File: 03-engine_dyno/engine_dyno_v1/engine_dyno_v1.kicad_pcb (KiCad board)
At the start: 4 copper layers, 101.3 x 69 mm, 91 parts, among them J1 Screw_Terminal_01x02, J4 Screw_Terminal_01x05, J5 Screw_Terminal_01x03, J6 Screw_Terminal_01x05, J7 Screw_Terminal_01x03, P1 J1B1211CCD, Q1 PMOS, U1 LMR51430XDDCR, U10 INA827AIDGKR, U11 74LVC1G17, U12 AD630ARZ, U13 ADS1120IPWR, U14 OPA192IDBVR, U15 OPA192IDBVR, U16 74LVC1G17, U2 TVS1800DRV, U3 TPS2115APWR, U4 TPS60403DBVRG4, U5 AD5689RBRUZ, U6 Teensy4.1, U7 INA827AIDGKR, U8 AD630ARZ, U9 ADS1120IPWR

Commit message: drc errors fixed
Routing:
- net /MCU/MOSI: track 78.0 -> 89.0 mm
- net Net-(U10-VOUT): track 32.2 -> 33.6 mm

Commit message: some silkscreen fancifications
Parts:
- moved C5 0.05 mm to (169.1, 86.9)
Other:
- outline, holes or cut-outs redrawn
- board text added: "EXC+"
- board text added: "EXC-"
- board text added: "MODEL1605 Input"
- board text added: "SIG+"
- board text added: "SIG-"

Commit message: im aboutta release
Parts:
- added H1: MountingHole, MountingHole:MountingHole_3.2mm_M3_DIN965, F.Cu at (108.5, 73.0)
- added H2: MountingHole, MountingHole:MountingHole_3.2mm_M3_DIN965, F.Cu at (108.7, 108.0)
- added H3: MountingHole, MountingHole:MountingHole_3.2mm_M3_DIN965, F.Cu at (194.4, 60.6)
- added H4: MountingHole, MountingHole:MountingHole_3.2mm_M3_DIN965, F.Cu at (194.6, 121.1)
- C37: moved to F.Cu
- moved C20 35.0 mm to (166.6, 96.2), turned to 0 degrees
- moved U16 31.2 mm to (167.2, 93.7), turned to 180 degrees
- moved R17 27.0 mm to (177.1, 90.3), turned to -90 degrees
- moved J7 20.8 mm to (189.3, 82.1), turned to 90 degrees
- moved R26 20.7 mm to (180.4, 90.3), turned to -90 degrees
- moved U11 19.8 mm to (174.5, 94.7), turned to 180 degrees
- moved R18 19.1 mm to (179.5, 93.6), turned to -90 degrees
- moved R12 19.0 mm to (181.0, 86.0), turned to 180 degrees
- moved C36 19.0 mm to (180.4, 82.8), turned to -90 degrees
- moved C25 17.0 mm to (173.8, 97.6), turned to 0 degrees
- moved C26 15.7 mm to (179.5, 96.0), turned to 90 degrees
- moved J5 14.3 mm to (189.6, 102.3), turned to 90 degrees
- moved C37 6.90 mm to (177.2, 98.7)
- moved R4 5.59 mm to (167.6, 88.6), turned to 90 degrees
- moved C3 5.14 mm to (171.8, 84.7)
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- renumbered Cboot1 to Cb
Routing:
- net /Hall1/HALL: track 46.7 -> 7.54 mm
- net /Hall2/HALL: track 37.0 -> 17.5 mm
- net /power/+5V_BUCK: track 0.00 -> 15.2 mm
- net Net-(C36-Pad2): track 5.77 -> 17.9 mm
- net /MCU/+5V_USB: track 47.4 -> 58.9 mm, vias 1 -> 2
- net /MCU/A16: track 12.3 -> 20.8 mm
- net Net-(U3-D1): track 6.87 -> 14.6 mm
- net /Hall1/SIG: track 11.9 -> 17.5 mm
- net Net-(P1-RCT): track 7.99 -> 12.2 mm
- net -5V: track 18.4 -> 22.4 mm, vias 6 -> 7
- net /MCU/MOSI: track 89.0 -> 92.1 mm
- net /MCU/SCK: track 52.4 -> 55.2 mm, vias 1 -> 3
- net /Model1605/BIAS_REF: track 43.8 -> 46.4 mm, vias 3 -> 5
- net /Model1605/OPA192_OUT: track 7.02 -> 9.48 mm
- net Net-(C16-Pad2): track 4.36 -> 6.73 mm
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- removed copper zone on F.Cu, net +5V
- removed copper zone on F.Cu, net /power/+5V_BUCK
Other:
- board size 101.3 x 69 mm -> 95 x 69 mm
- board text added: "12V BATT"
- board text added: "ETHERNET"
- board text added: "GND"
- board text added: "HALL EFFECT 1"
- board text added: "HALL EFFECT 2"
- board text added: "JUSTIN LIAO ENGINE DYNO V1 BAJA JHU"
- board text added: "PWR"
- board text added: "SIG"
- board text added: "TMNR-5KM Input"
- board text added: "USB"

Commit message: polished
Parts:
- L1: value 10u -> 10uH; footprint Inductor_SMD:L_0402_1005Metric -> engine_dyno:WE-MAPI_3020
- moved Cb 3.76 mm to (179.6, 79.8), turned to 90 degrees
- moved L1 1.86 mm to (176.2, 83.2)
- moved C5 1.62 mm to (174.1, 87.5), turned to -90 degrees
- moved C4 0.96 mm to (170.3, 91.6), turned to 90 degrees
- moved C2 0.73 mm to (172.7, 81.4)
- moved H4 0.15 mm to (194.4, 121.1)
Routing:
- net Net-(U1-CB): track 2.65 -> 5.41 mm
- net Net-(U1-SW): track 7.36 -> 9.58 mm
- net Net-(U4-CFLY+): track 2.64 -> 4.22 mm
- net /power/+5V_BUCK: track 15.2 -> 16.2 mm
- net Net-(U4-CFLY-): track 6.31 -> 5.53 mm

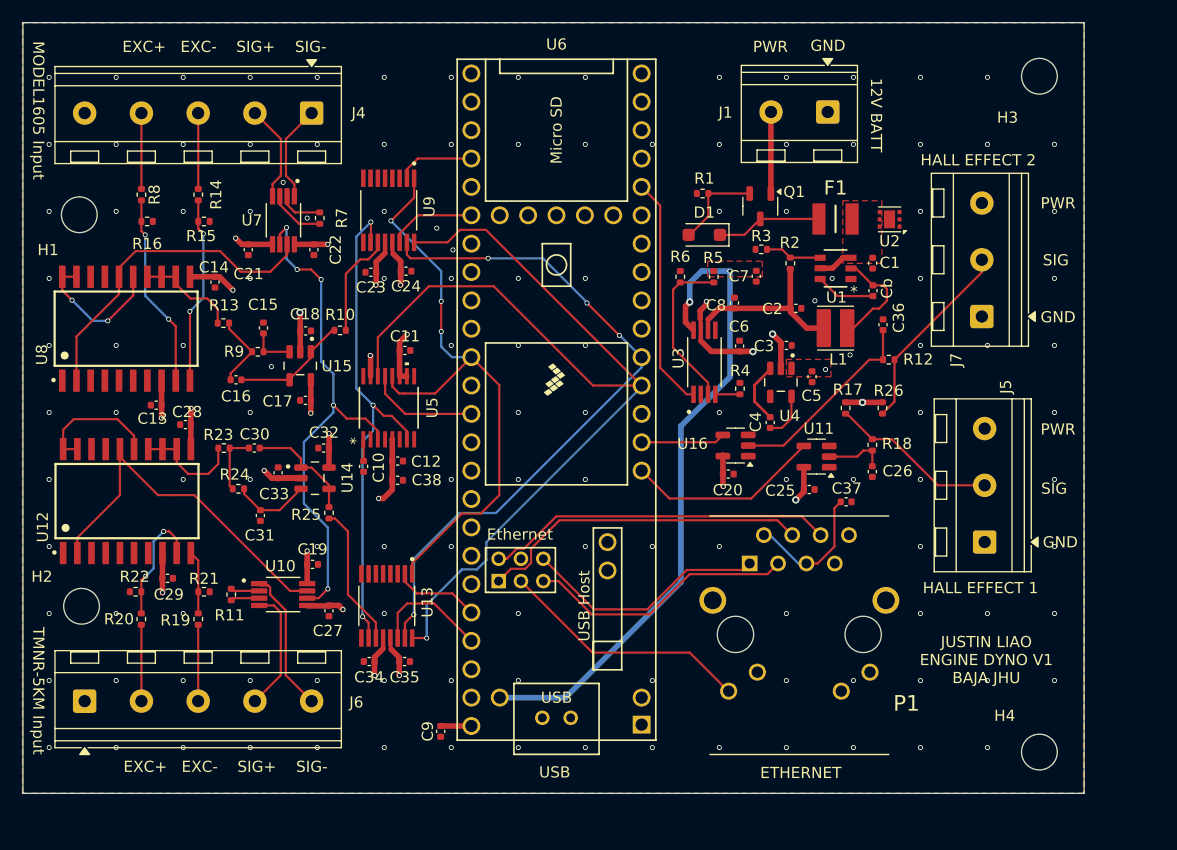
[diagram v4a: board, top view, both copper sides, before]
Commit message: fillet, plated holes, via size
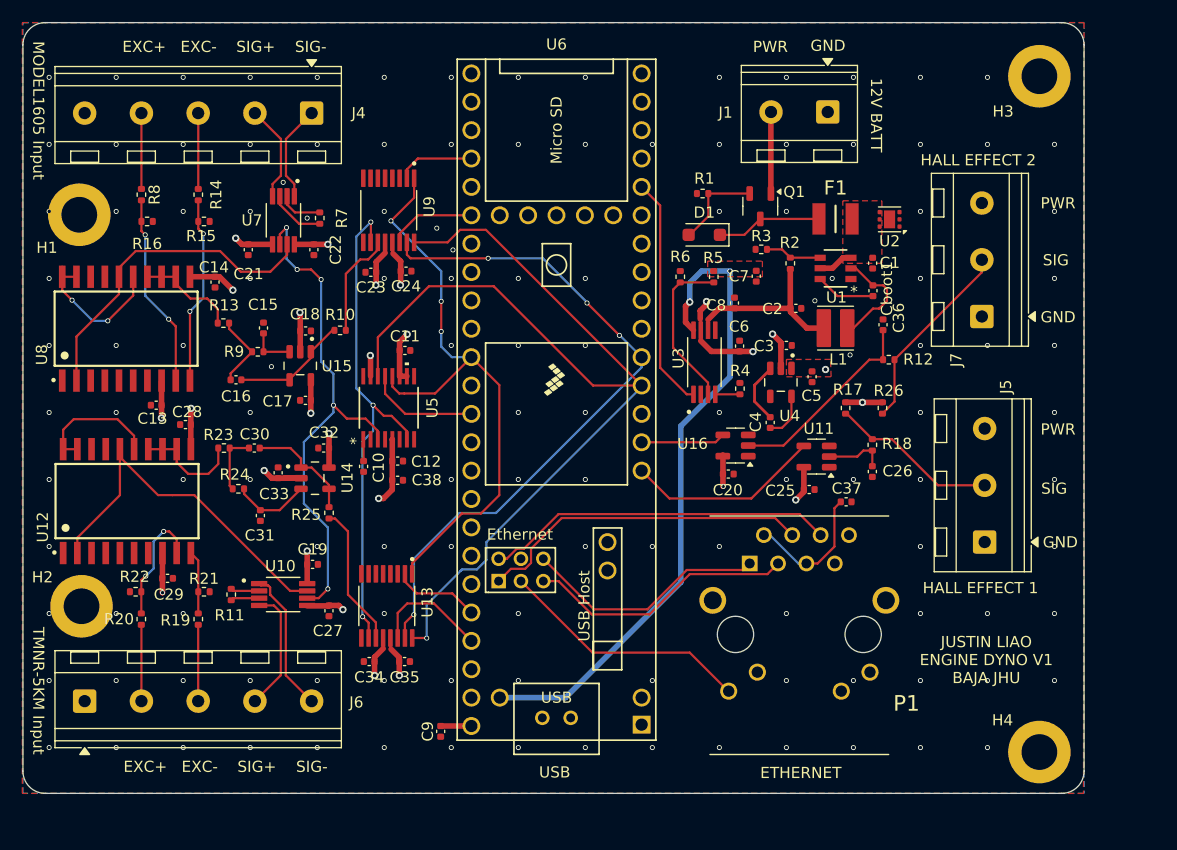
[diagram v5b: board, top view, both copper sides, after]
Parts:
- H1, H2, H3, H4: footprint MountingHole:MountingHole_3.2mm_M3_DIN965 -> MountingHole:MountingHole_3.2mm_M3_DIN965_Pad
- renumbered Cb to Cboot1
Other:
- outline, holes or cut-outs redrawn

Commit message: resolved review sheet issues
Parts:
- added G***: BJR_LOGO, 22XT_Main:BJR_LOGO, F.Cu at (189.1, 118.0)
- moved C8 1.00 mm to (166.2, 80.9)
- renumbered Cboot1 to Cb1
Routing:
- net /MCU/TD+: track 22.1 -> 24.1 mm
- net /MCU/RD+: track 30.0 -> 31.0 mm
- net GND: vias 129 -> 125
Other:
- board text added: "Blue Jay Racing @ Johns Hopkins 23XT Engine Dyno Rev 1"
- board text added: "Gwen Tran Cyan Brown Sophie Noureddine"
- board text added: "Justin Liao"
- board text removed: "JUSTIN LIAO ENGINE DYNO V1 BAJA JHU"
